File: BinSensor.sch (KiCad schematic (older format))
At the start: 20 parts

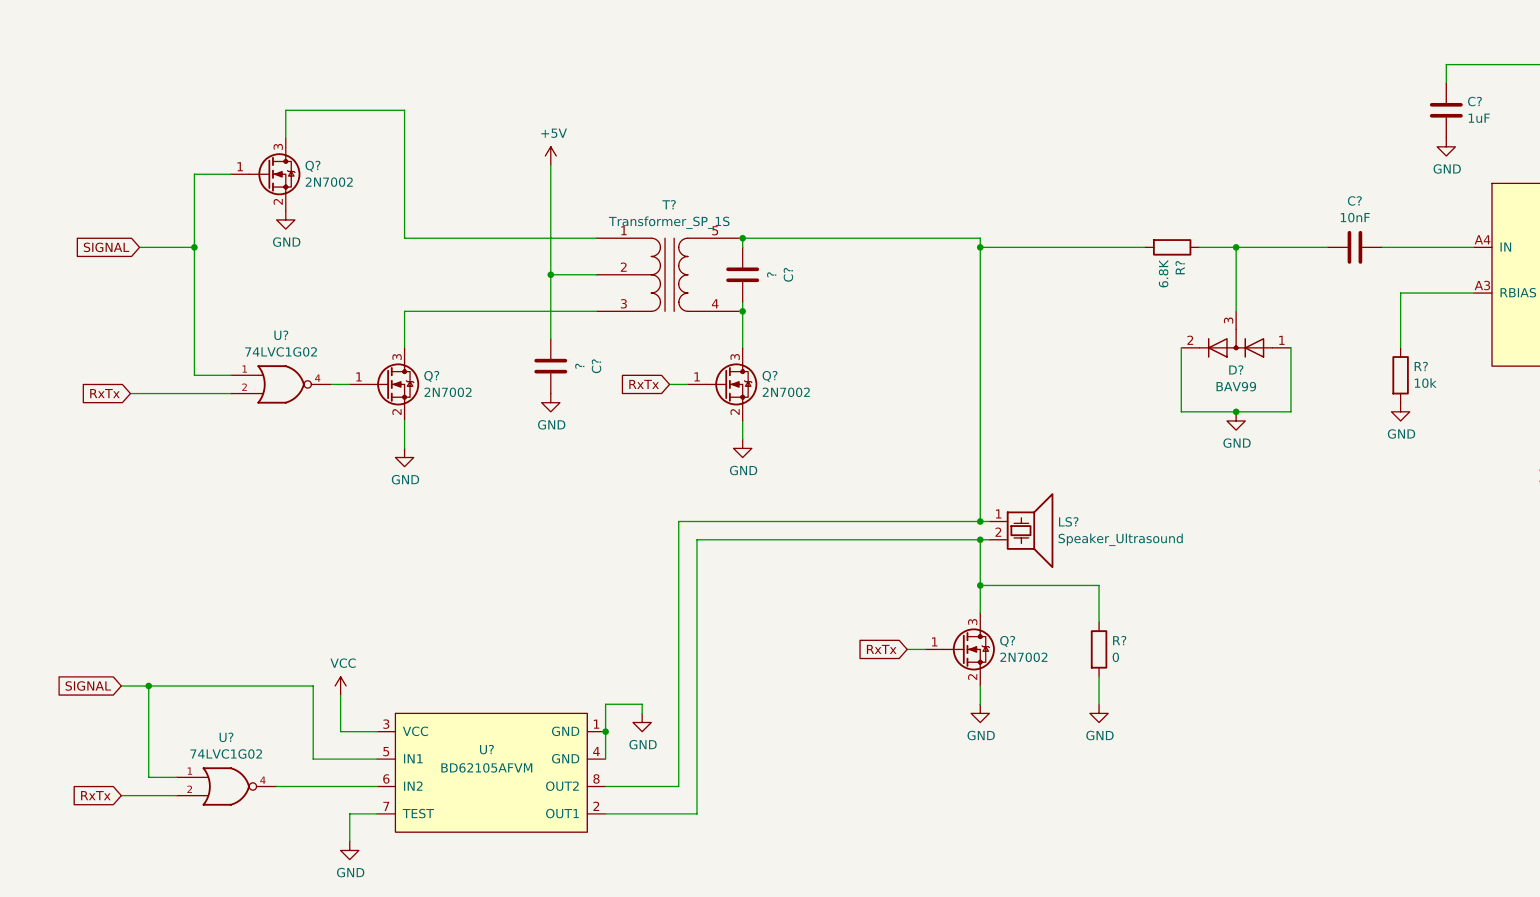
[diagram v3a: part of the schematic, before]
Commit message: Added jumpers and pulldown resistors for the MOSFETs.
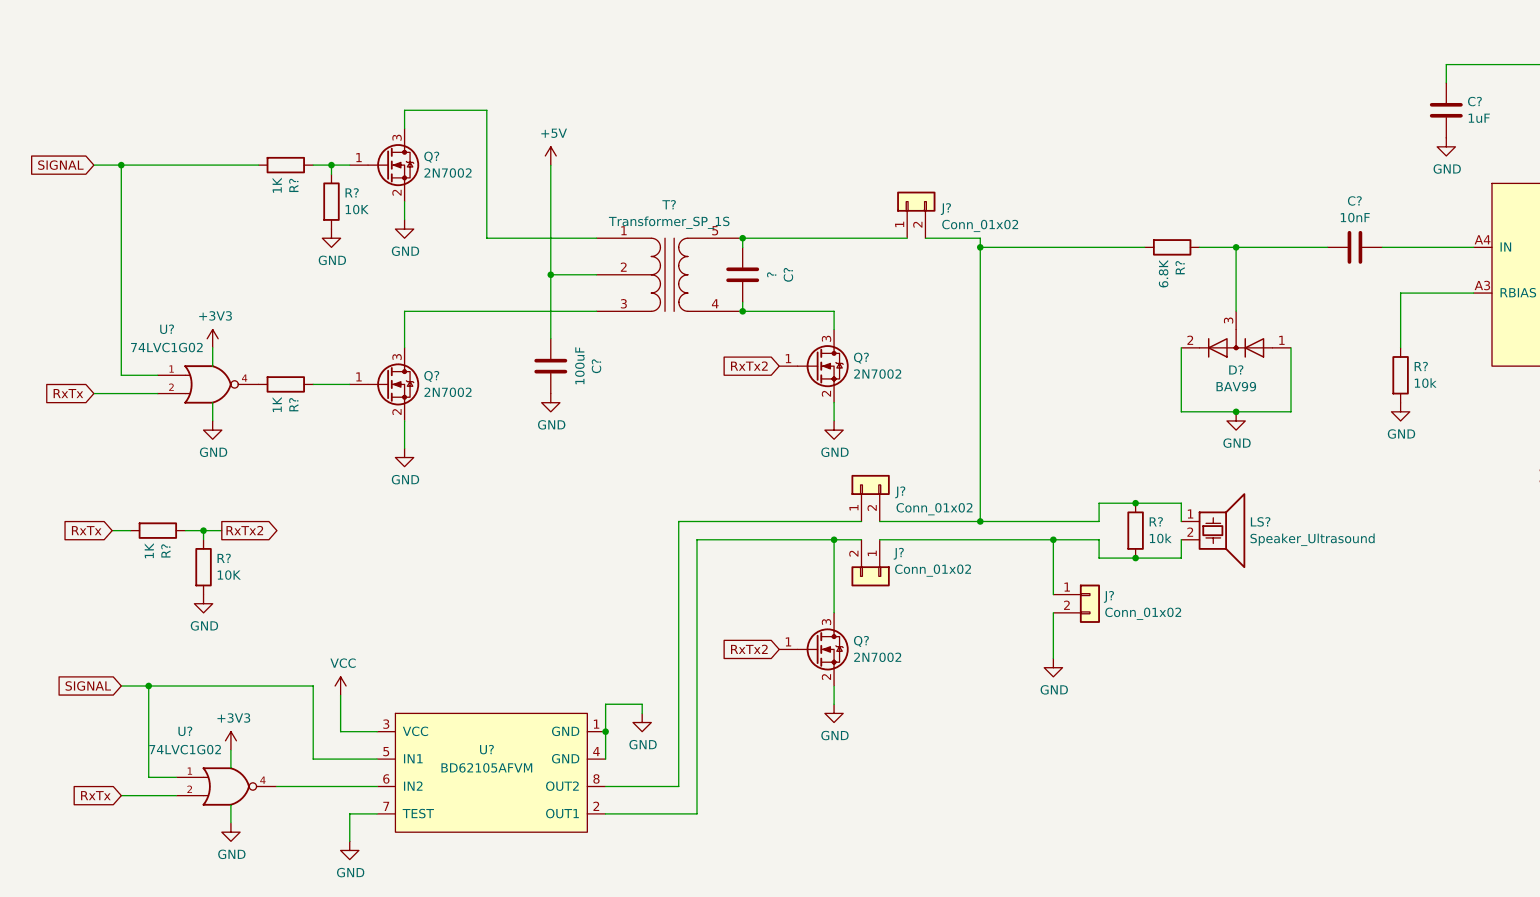
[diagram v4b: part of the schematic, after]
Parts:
- removed R?: 0, symbol Device:R
- added J? (x4): Conn_01x02, symbol Connector_Generic:Conn_01x02
- added R? (x3): 1K, symbol Device:R
- added R? (x2): 10K, symbol Device:R
- added R?: 10k, symbol Device:R
- C?: value ? -> 100uF
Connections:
- net VCC is gone; now on net +3V3: U?.3 (VCC), U?.5 (VCC), U?.5 (VCC)
- net GND: now also J?.2 (Pin_2), R?.2, R?.2
- net RxTx: now also R?.2; no longer Q?.1 (G), Q?.1 (G)
- net SIGNAL: now also R?.2; no longer Q?.1 (G)
- net at Q?.3 (D), U?.2 (OUT1): now also J?.2 (Pin_2); no longer LS?.2
- net at Q?.1 (G): now also R?.1; no longer U?.4
- new net: C?.2, J?.1 (Pin_1), T?.5 (S2)
- new net: J?.2 (Pin_2), J?.2 (Pin_2), LS?.1, R?.1, R?.2
- new net: J?.1 (Pin_1), J?.1 (Pin_1), LS?.2, R?.2
- new net: Q?.1 (G), R?.1, R?.1
- new net: J?.1 (Pin_1), U?.8 (OUT2)
- new net: R?.2, U?.4
- new net RxTx2: Q?.1 (G), Q?.1 (G), R?.1, R?.1
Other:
- moved on the sheet: LS?, Q?, U?
